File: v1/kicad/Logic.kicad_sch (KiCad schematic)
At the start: 159 parts, among them J2 X, J5 Y, J6 Sync, P1 4k7, P10 10k, P11 200R, P12 20k, P2 47k, P3 10k, P4 47k, P5 47k, P6 10k, P8 200R, P9 2k, Q1 BC558C, Q2 BC548C, Q3 BD139, Q4 BD140, Q5 BD139, Q6 BD140, SW10 SP3T, SW11 SP4T, SW12 DP3T, SW13 SP4T, SW2 BTN, SW3 DP4T Rot, SW4 DP3T Rot, SW5 DPST, SW6 3PDT, SW7 SP2T, SW8 SPDT, SW9 DPDT, U1 NE555P, U10 OPA2277, U11 ADG419BN, U12 ADG419BN, U13 CD40106B, U16 OPA2277, U2 OPA2277, U4 TL072, U5 TL072, U6 CD4520, U7 ADG419BN

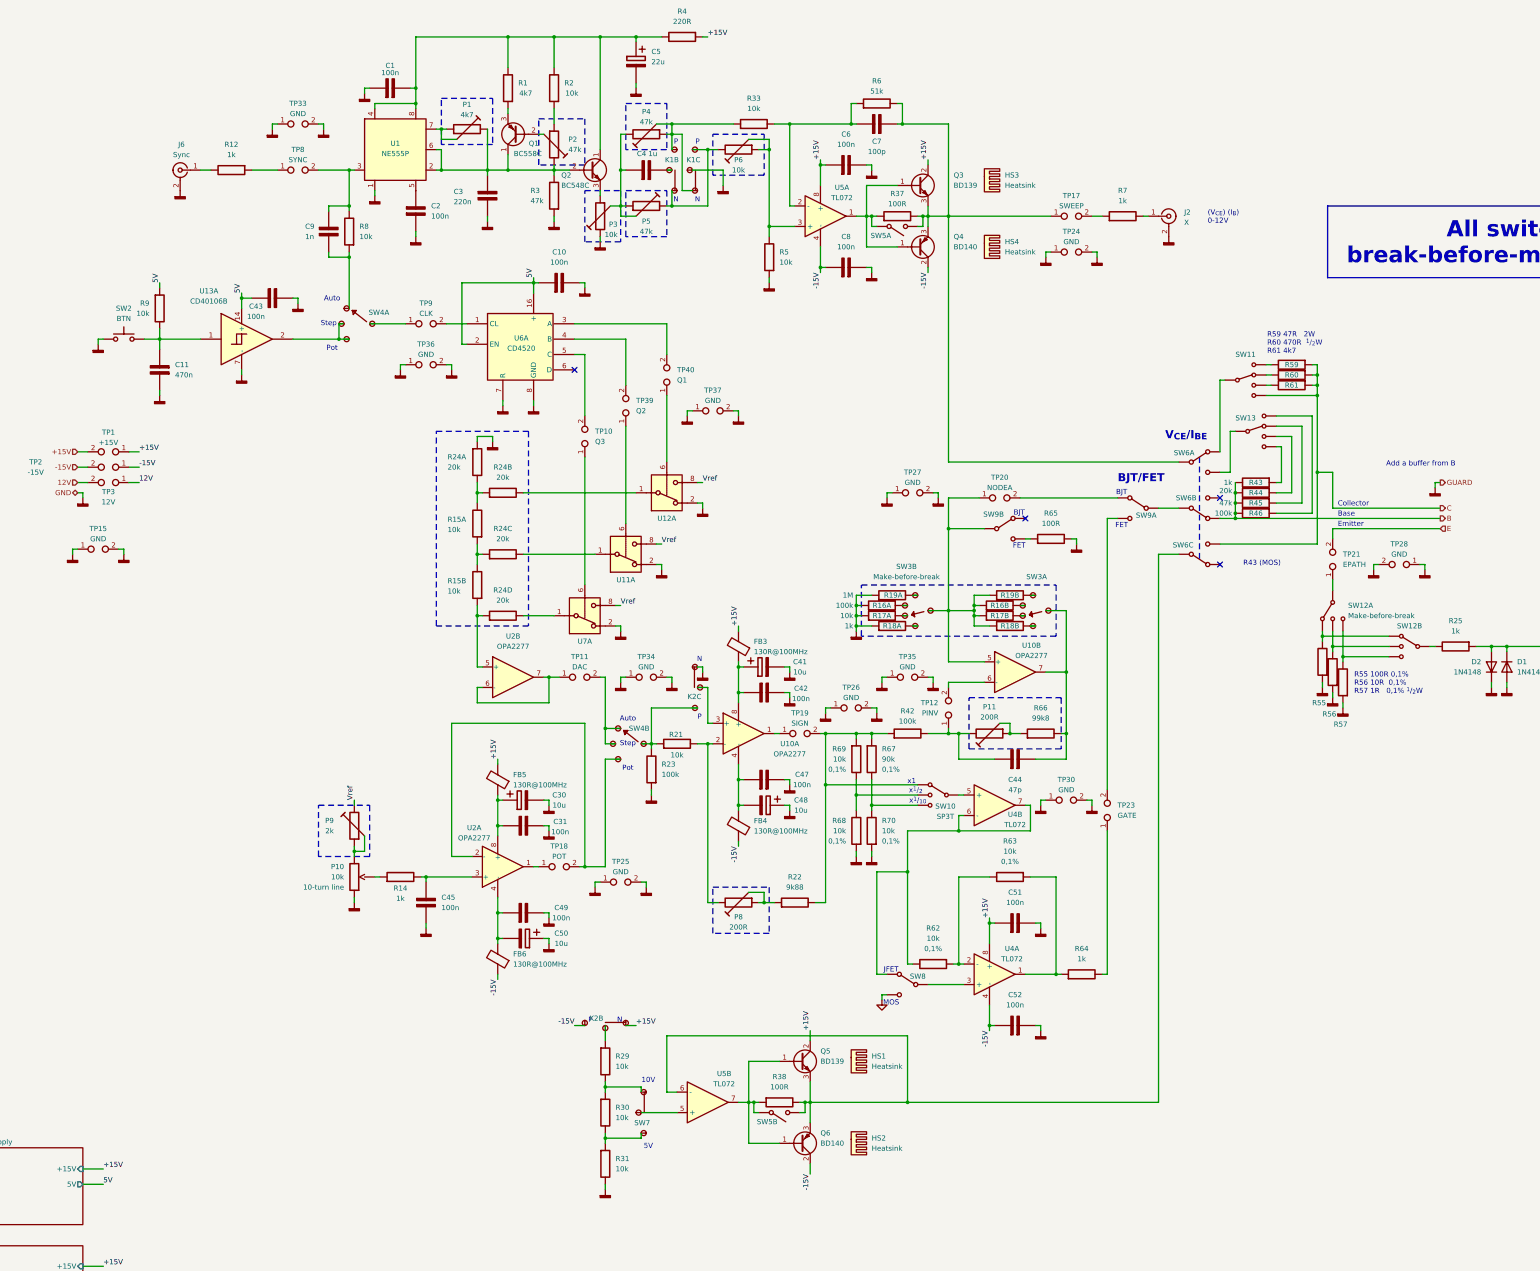
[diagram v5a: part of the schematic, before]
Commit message: Fixed mistakes and made making a BOM easier
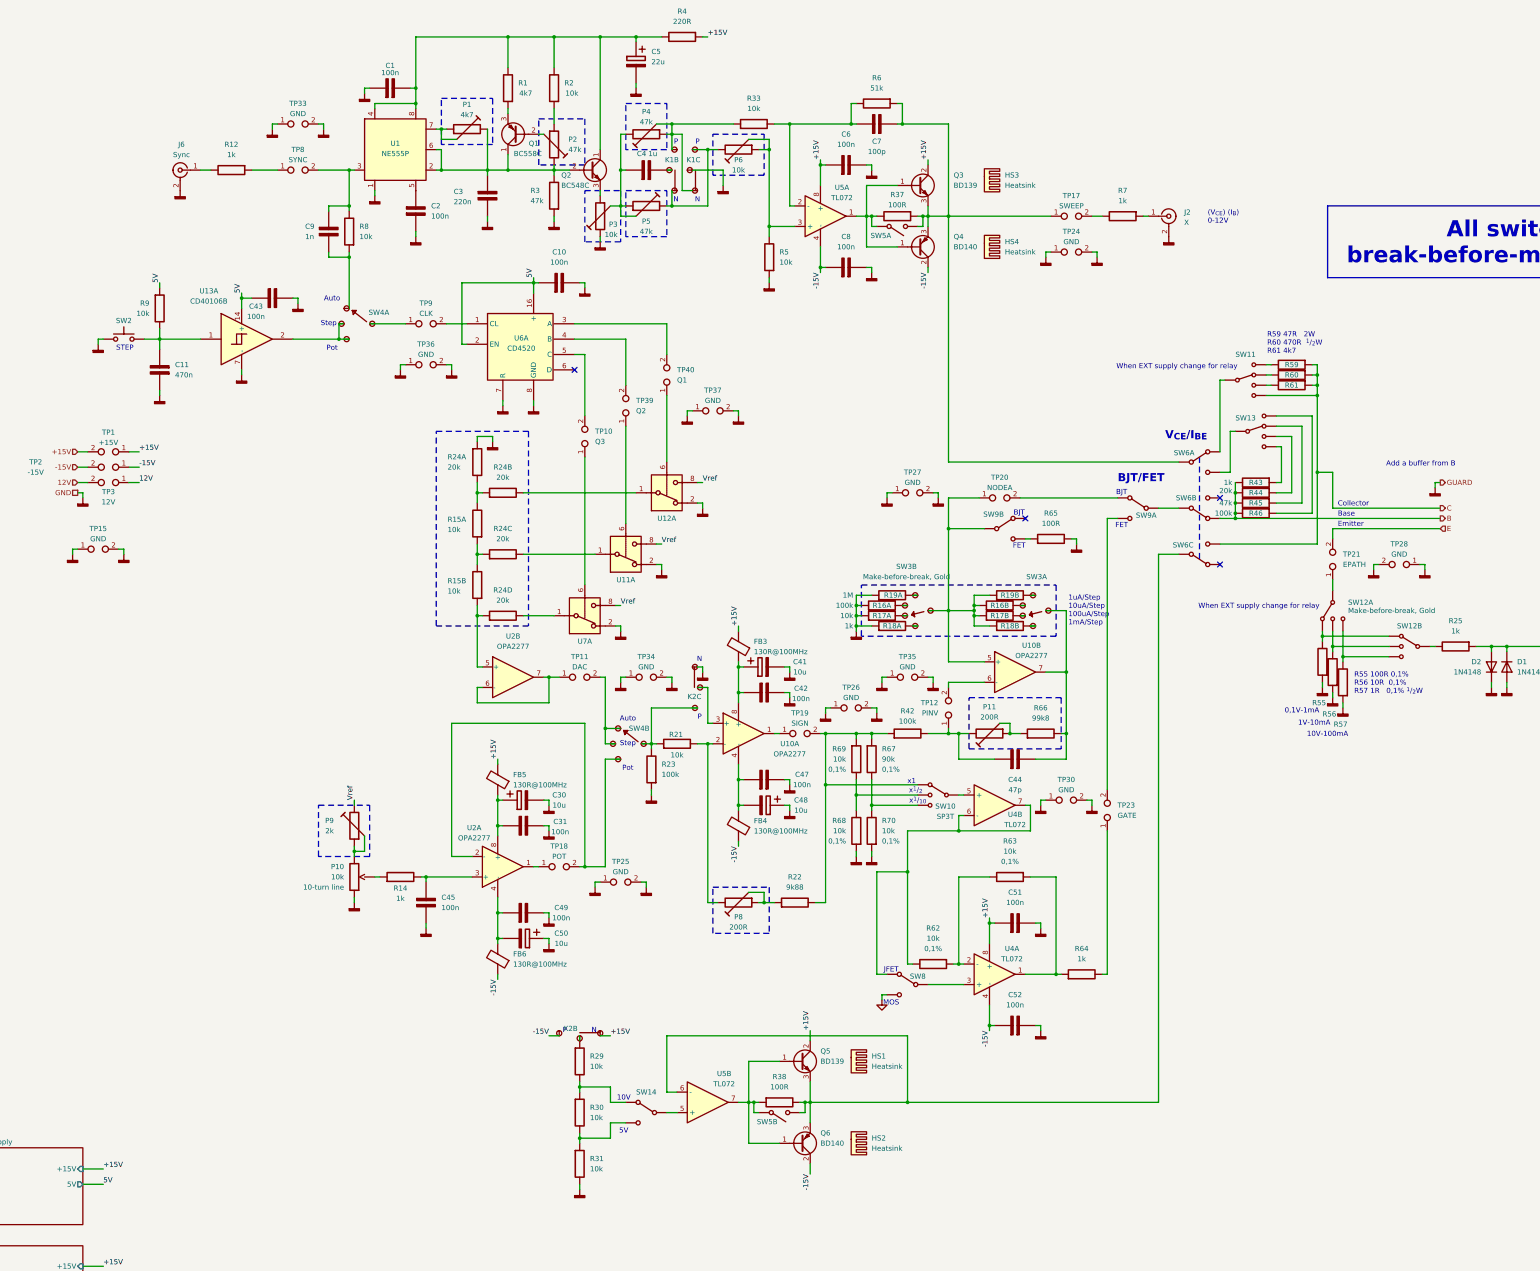
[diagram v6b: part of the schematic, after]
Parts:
- removed SW7: SP2T, symbol custom:SW-SPDT-Flat_Basic
- added SW14: SPDT, symbol custom:SW-SPDT_Basic
- C3, C30, C4, C41, C48, C50, J2, J5, J6, K1, K2, P1, P10, P11, P12, P2, P3, P4, P5, P6, P8, P9, R15, R16, R17, R18, R19, R24, R28, R55, R56, R57, R62, R63, R67, R68, R69, R70, SW10, SW11, SW12, SW13, SW2, SW3, SW4, SW5, SW6, SW8, SW9: Spend (none) -> $$$
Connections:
- net +15V: now also C51.1, C6.1, K2.5, R4.1; no longer C51., C6., K2., R4.
- net -15V: now also C52.1, C8.1, K2.3; no longer C52., C8., K2.
- net 5V: now also C10.1, C43.2, R9.1; no longer C10., C43., R9.
- net B: now also R43.2, R44.2, R45.2, R46.2, SW6.5 (A); no longer R43., R44., R45., R46., SW6.1 (A)
- net C: now also R59.1, R60.1, R61.1, SW11.5 (4), SW6.9 (C); no longer R59., R60., R61., SW11.4, SW6.3 (C)
- net GND: now also C1.1, C10.2, C11.1, C2.2, C3.2, C31.1, C42.1, C43.1, C45.2, C47.2, C49.2, C5.2, C51.2, C52.2, C6.2, C8.2, K1.7, K2.8, P10.2, P3.1, R23.1, R28.2, R3.1, R31.2, R5.1, R55.1, R56.1, R57.1, R65.2, R68.1, R70.1; no longer C1., C10., C11., C2., C3., C31., C42., C43., C45., C47., C49., C5., C51., C52., C6., C8., K1., K2., P10., P3., R23., R28., R3., R31., R5., R55., R56., R57., R65., R68., R70.
- net Vref: now also P9.1; no longer P9.
- net at R17.2: now also SW3.8 (A); no longer SW3.1 (A)
- net at Q5.3 (E), Q6.3 (E), U5.6 (-): now also R38.2, SW5.4 (A), SW6.7 (B); no longer R38., SW5.1 (A), SW6.2 (B)
- net at Q5.1 (B), Q6.1 (B), U5.7: now also R38.1, SW5.3 (B); no longer R38., SW5.2 (B)
- net at C50.2, FB6.2, U2.4 (-): now also C49.1; no longer C49.
- net at R16.2: now also SW3.9 (A); no longer SW3.1 (A)
- net at Q1.1 (C), Q2.2 (B), U1.2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: now also C3.1, P1.1, P2.1, R3.2; no longer C3., P1., P2., R3.
- net at U1.7: now also P1.2, P1.3; no longer P1.
- net at TP9.1: now also SW4.1 (B); no longer SW4.2 (B)
- net at SW2.1, U13.1: now also C11.2, R9.2; no longer C11., R9.
- net at Q1.3 (E): now also R1.1; no longer R1.
- net at TP18.2, U2.2 (-): now also SW4.8; no longer SW4.3 (C)
- net at C30.1, FB5.1, U2.8 (+): now also C31.2; no longer C31.
- net at SW11.2 (1): now also R59.2; no longer R60.
- net at J6.1 (In): now also R12.2; no longer R12.
- net at TP8.1: now also R12.1; no longer R12.
- net at C41.1, FB3.1, U10.8 (+): now also C42.2; no longer C42.
- net at C48.2, FB4.2, U10.4 (-): now also C47.1; no longer C47.
- net at TP8.2, U1.3: now also C9.1, R8.2; no longer C9., R8.
- net at U1.5: now also C2.1; no longer C2.
- net at U5.5 (+): now also SW14.1 (B)
- net at Q1.2 (B): now also P2.3; no longer P2.
- net at D1.1 (K), D2.2 (A), U16.3 (+): now also R25.1; no longer R25.
- net at R16.4, R17.4, R18.4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: now also SW3.6 (B); no longer SW3.2 (B)
- net at SW4.3 (A), U13.2: now also SW4.4 (C); no longer SW4.1 (A)
- net at R19.3: now also SW3.5 (C); no longer SW3.3 (C)
- net at SW8.2 (A), U4.6 (-), U4.7: now also R62.2; no longer R62.
- net at SW13.4: now also R44.1; no longer R44.
- net at U10.3 (+): now also K2.7; no longer K2.
- net at Q3.1 (B), Q4.1 (B), U5.1: now also R37.2, SW5.1 (B); no longer R37., SW5.2 (B)
- net at TP22.2: now also R27.1; no longer R27.
- net at J5.1 (In): now also R27.2; no longer R27.
- net at SW6.1 (B): now also C7.2, Q3.3 (E), Q4.3 (E), R37.1, R6.1, SW5.2 (A), TP17.1; no longer SW11.3
- net at SW6.3 (C): now also SW13.1 (3); no longer SW13.3
- net at Q2.3 (E): now also P3.2; no longer P3.
- net at SW3.1 (B): now also C44.2, R66.2, U10.7; no longer R17.3
- net at TP23.1: now also R64.2; no longer R64.
- net at R16.3: now also SW3.4 (A); no longer SW3.1 (A)
- net at R18.3: now also SW3.2 (A); no longer SW3.1 (A)
- net at R19.2: now also SW3.10 (C); no longer SW3.3 (C)
- net at SW9.6 (C): now also R65.1; no longer R65.
- net at TP22.1, U16.1: now also R26.2; no longer R26.
- net at TP11.2: now also SW4.6 (A), SW4.7 (A); no longer SW4.1 (A)
- net at SW11.1 (3): now also SW6.2 (A); no longer R59.
- net at R18.2: now also SW3.7 (A); no longer SW3.1 (A)
- net at SW13.2 (1): now also R46.1; no longer R45.
- net at SW9.1 (B): now also SW6.4 (B); no longer SW6.2 (B)
- net at SW12.3 (2): now also R56.2, SW12.7 (2); no longer TP21.1
- net at J2.1 (In): now also R7.1; no longer R7.
- net at TP17.2: now also R7.2; no longer R7.
- net at SW11.4: now also R61.2; no longer R61.
- new net: K1.3, K1.8, P4.2, P4.3, R33.1
- new net: C4.2, K1.4
- new net: K1.5, K1.6, P5.1, P6.1
- new net: K2.4, R29.1
- new net: R29.2, R30.1, SW14.2 (A)
- new net: C44.1, P11.1, R42.2, TP12.1
- new net: R22.2, R42.1, R67.1, R69.1, SW10.2 (1), TP19.2
- new net: C7.1, R33.2, R6.2, U5.2 (-)
- new net: C1.2, C5.1, Q2.1 (C), R1.2, R2.2, R4.2, U1.4, U1.8
- new net: R68.2, R69.2, SW10.3 (2)
- new net: R67.2, R70.2, SW10.4
- new net: C45.1, R14.2, U2.3 (+)
- new net: K2.6, R21.1, R23.2, SW4.5 (B)
- new net: P8.1, R21.2, U10.2 (-)
- new net: C4.1, P3.3, P4.1, P5.2, P5.3
- new net: R60.2, SW11.3 (2)
- new net: R25.2, SW12.5 (3)
- new net: R55.2, SW12.2 (1), SW12.6 (1)
- new net: R57.2, SW12.4, SW12.8 (4)
- new net: P10.1, P9.2, P9.3
- new net: P10.3, R14.1
- new net: C9.2, R8.1, SW4.2 (A)
- new net: P2.2, R2.1
- new net: R43.1, SW13.5 (4)
- new net: R17.3, SW3.3 (A)
- new net: P11.2, P11.3, R66.1
- new net: R63.1, R64.1, U4.1
- new net: R30.2, R31.1, SW14.3 (C)
- new net: R62.1, R63.2, U4.2 (-)
- new net: P12.1, R28.1, U16.2 (-)
- new net: R45.1, SW13.3 (2)
- new net: P12.2, P12.3, R26.1
- new net: P6.2, P6.3, R5.2, U5.3 (+)
- new net: SW12.1 (3), TP21.1
- new net: P8.2, P8.3, R22.1
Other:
- note added: "0,1V-1mA"
- note added: "10V-100mA"
- note added: "1V-10mA"
- note added: "1uA/Step 10uA/Step 100uA/Step 1mA/Step"
- note added: "STEP"
- note added: "When EXT supply change for relay"
- note removed: "R43 (MOS)"
- moved on the sheet: K2B, R29, R30, R31, R37, R6, R7
